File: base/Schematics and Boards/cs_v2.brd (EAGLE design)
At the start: 25.4 x 25.4 mm, 81 parts, among them J101 J-JTAG-CORTEX-NEEDLE6, J301 HIROSE-DF40_44-PIN_CONNECTORS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, J302 HIROSE-DF40_30-PIN_CONNECTORS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, Q201 FK3303010L, Q202 FK3303010L, Q203 FK3303010L, Q204 DMG3415UFY4Q-7, U1 AT25SF641-MHB-T, U101 ATSAMD51, U201 COULOMB-MAX17262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

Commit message: Ready to route
interior planes placed, but not exterior. Layering stackup setup similar to the way JLC recommends (hopefully standard)
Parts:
- moved T_RX 12.8 mm to (17.9, 6.60), flipped to the top
- moved T_TX 7.90 mm to (15.1, 6.58), flipped to the top
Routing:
- removed copper zone on layer 15, net +3V3_STOR
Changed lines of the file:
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@@
 <class number="0" name="default" width="0" drill="0">
 </class>
-<class number="1" name="power_3v3" width="0.3048" drill="0">
+<class number="1" name="power_3v3" width="0.254" drill="0">
 </class>
 <class number="5" name="10_mil" width="0.254" drill="0">
@@
 <autorouter>
 <pass name="Default">
-<param name="RoutingGrid" value="50mil"/>
-<param name="AutoGrid" value="1"/>
-<param name="Efforts" value="0"/>
+<param name="RoutingGrid" value="1mil"/>
+<param name="AutoGrid" value="0"/>
+<param name="Efforts" value="2"/>
 <param name="TopRouterVariant" value="1"/>
 <param name="tpViaShape" value="round"/>
 <param name="PrefDir.1" value="a"/>
 <param name="PrefDir.2" value="0"/>
-<param name="PrefDir.3" value="0"/>
+<param name="PrefDir.3" value="*"/>
 <param name="PrefDir.4" value="0"/>
 <param name="PrefDir.5" value="0"/>
@@
 <param name="PrefDir.12" value="0"/>
 <param name="PrefDir.13" value="0"/>
-<param name="PrefDir.14" value="0"/>
+<param name="PrefDir.14" value="*"/>
 <param name="PrefDir.15" value="0"/>
 <param name="PrefDir.16" value="a"/>
@@
 <attribute name="VALUE" x="1.27" y="20.447" size="0.6096" layer="28" font="vector" ratio="20" rot="MR90" align="top-center"/>
 </element>
-<element name="T_RX" library="TestPoints" package="TP06R" package3d_urn="urn:adsk.eagle:package:27954/1" value="TPTP06R" x="6.35" y="1.0668" smashed="yes" rot="MR0">
-<attribute name="NAME" x="7.4016" y="1.635" size="0.8128" layer="26" rot="MR0"/>
-<attribute name="POPULARITY" value="1" x="-20.32" y="-48.4632" size="1.778" layer="28" rot="MR0" display="off"/>
-<attribute name="TP_SIGNAL_NAME" value="" x="6.35" y="-1.4732" size="1" layer="38" rot="MR0"/>
-</element>
-<element name="T_TX" library="TestPoints" package="TP06R" package3d_urn="urn:adsk.eagle:package:27954/1" value="TPTP06R" x="9.652" y="0.8636" smashed="yes" rot="MR0">
-<attribute name="NAME" x="10.7036" y="1.4572" size="0.8128" layer="26" rot="MR0"/>
-<attribute name="POPULARITY" value="1" x="-22.098" y="-48.6664" size="1.778" layer="28" rot="MR0" display="off"/>
-<attribute name="TP_SIGNAL_NAME" value="" x="9.652" y="-1.6764" size="1" layer="38" rot="MR0"/>
+<element name="T_RX" library="TestPoints" package="TP06R" package3d_urn="urn:adsk.eagle:package:27954/1" value="TPTP06R" x="17.907" y="6.604" smashed="yes">
+<attribute name="NAME" x="16.8046" y="7.1468" size="0.8128" layer="25"/>
+<attribute name="POPULARITY" value="1" x="44.577" y="-42.926" size="1.778" layer="27" display="off"/>
+<attribute name="TP_SIGNAL_NAME" value="" x="17.907" y="4.064" size="1" layer="37"/>
+</element>
+<element name="T_TX" library="TestPoints" package="TP06R" package3d_urn="urn:adsk.eagle:package:27954/1" value="TPTP06R" x="15.113" y="6.5786" smashed="yes">
+<attribute name="NAME" x="13.2232" y="7.0198" size="0.8128" layer="25"/>
+<attribute name="POPULARITY" value="1" x="46.863" y="-42.9514" size="1.778" layer="27" display="off"/>
+<attribute name="TP_SIGNAL_NAME" value="" x="15.113" y="4.0386" size="1" layer="37"/>
 </element>
 <element name="U101" library="Processors" package="TFBGA120" value="ATSAMD51" x="16.3068" y="13.1826" smashed="yes" rot="MR90">
@@
 <contactref element="J301" pad="5"/>
 <polygon width="0.1524" layer="2">
-<vertex x="-49.53" y="31.115"/>
-<vertex x="-49.53" y="-0.635"/>
-<vertex x="-16.383" y="-0.635"/>
-<vertex x="-16.383" y="31.115"/>
+<vertex x="-3.81" y="27.94"/>
+<vertex x="-3.81" y="-3.81"/>
+<vertex x="29.337" y="-3.81"/>
+<vertex x="29.337" y="27.94"/>
 </polygon>
 <contactref element="S101" pad="2_2"/>
@@
 <contactref element="U1" pad="4"/>
 <polygon width="0.1524" layer="16">
-<vertex x="-51.435" y="33.02"/>
-<vertex x="-51.435" y="-2.54"/>
-<vertex x="-14.478" y="-2.54"/>
-<vertex x="-14.478" y="33.02"/>
+<vertex x="-57.15" y="33.655"/>
+<vertex x="-57.15" y="-3.175"/>
+<vertex x="-18.288" y="-3.175"/>
+<vertex x="-18.288" y="33.655"/>
 </polygon>
 <polygon width="0.1524" layer="1">
-<vertex x="-47.625" y="29.21"/>
-<vertex x="-47.625" y="0.635"/>
-<vertex x="-18.288" y="0.635"/>
-<vertex x="-18.288" y="29.21"/>
+<vertex x="-52.705" y="29.845"/>
+<vertex x="-52.705" y="1.27"/>
+<vertex x="-23.368" y="1.27"/>
+<vertex x="-23.368" y="29.845"/>
 </polygon>
 <wire x1="21.9274" y1="21.209" x2="20.371" y2="23.9522" width="0" layer="19" extent="1-16"/>
@@
 <contactref element="J302" pad="14"/>
 <polygon width="0.1524" layer="15">
-<vertex x="54.61" y="31.242"/>
-<vertex x="54.61" y="12.7"/>
-<vertex x="76.2" y="12.7"/>
-<vertex x="76.2" y="31.242"/>
+<vertex x="-5.08" y="29.337"/>
+<vertex x="-5.08" y="-5.08"/>
+<vertex x="31.115" y="-5.08"/>
+<vertex x="31.115" y="29.337"/>
 </polygon>
 <contactref element="T_CPU" pad="TP"/>
@@
 <contactref element="U205" pad="B1"/>
 <contactref element="C208" pad="1"/>
-<polygon width="0.1524" layer="15">
-<vertex x="76.2" y="-6.858"/>
-<vertex x="57.404" y="-6.858"/>
-<vertex x="57.404" y="12.319"/>
-<vertex x="76.2" y="12.319"/>
-</polygon>
 <contactref element="U1" pad="8"/>
 <contactref element="T_STR" pad="TP"/>
@@
 <contactref element="J302" pad="15"/>
 <wire x1="15.80681875" y1="10.182603125" x2="16.637003125" y2="24.273" width="0" layer="19" extent="16-16"/>
-<wire x1="9.652" y1="0.8636" x2="15.80681875" y2="10.182603125" width="0" layer="19" extent="16-16"/>
+<wire x1="15.113" y1="6.5786" x2="15.80681875" y2="10.182603125" width="0" layer="19" extent="16-16"/>
 </signal>
 <signal name="DBG_SERIAL_RX">
@@
 <contactref element="J302" pad="17"/>
 <wire x1="15.306821875" y1="9.68260625" x2="17.037003125" y2="24.273" width="0" layer="19" extent="16-16"/>
-<wire x1="6.35" y1="1.0668" x2="15.306821875" y2="9.68260625" width="0" layer="19" extent="16-16"/>
+<wire x1="17.907" y1="6.604" x2="15.306821875" y2="9.68260625" width="0" layer="19" extent="16-16"/>
 </signal>
 <signal name="JTAG_NRESET">
@@
 <wire x1="4.417" y1="18.197" x2="5.969" y2="18.611" width="0" layer="19" extent="16-16"/>
 </signal>
-<signal name="VREG_LX1" class="1">
+<signal name="VREG_LX1">
 <contactref element="U203" pad="A1"/>
 <contactref element="L201" pad="1"/>
 <wire x1="8.3185" y1="12.2428" x2="8.3502" y2="14.8178" width="0" layer="19" extent="16-16"/>
 </signal>
-<signal name="VREG_LX2" class="1">
+<signal name="VREG_LX2">
 <contactref element="L201" pad="2"/>
 <contactref element="U203" pad="C1"/>
 <wire x1="5.8039" y1="12.2428" x2="7.5502" y2="14.8178" width="0" layer="19" extent="16-16"/>
 </signal>
-<signal name="VREG_BIAS" class="1">
+<signal name="VREG_BIAS">
 <contactref element="C204" pad="1"/>
 <contactref element="U203" pad="A3"/>
@@
 <wire x1="19.304" y1="0.7874" x2="8.030003125" y2="4.715" width="0" layer="19" extent="1-1"/>
 </signal>
-<signal name="VDD_DBG_JMP" class="5">
+<signal name="VDD_DBG_JMP" class="1">
 <contactref element="Q204" pad="1"/>
 <contactref element="R204" pad="2"/>
@@
 <wire x1="8.57" y1="20.209" x2="10.3886" y2="22.225" width="0" layer="19" extent="16-16"/>
 </signal>
-<signal name="VREG_IN" class="5">
+<signal name="VREG_IN" class="1">
 <contactref element="U203" pad="A2"/>
 <contactref element="C202" pad="1"/>
@@
 <wire x1="8.0906" y1="15.113" x2="9.6012" y2="15.0368" width="0" layer="19" extent="1-1"/>
 </signal>
-<signal name="+3V3_TEMP" class="1">
+<signal name="+3V3_TEMP">
 <contactref element="U206" pad="A1"/>
 <contactref element="U206" pad="B1"/>
@@
 <wire x1="21.664" y1="13.8684" x2="23.2664" y2="12.3952" width="0" layer="19" extent="1-16"/>
 </signal>
-<signal name="+3V3_TEMP_SENSE" class="1">
+<signal name="+3V3_TEMP_SENSE">
 <contactref element="U206" pad="A2"/>
 <contactref element="U206" pad="B2"/>
@@
 <wire x1="14.637003125" y1="24.273" x2="14.237003125" y2="24.273" width="0" layer="19" extent="16-16"/>
 </signal>
-<signal name="VDD_SW" class="5">
+<signal name="VDD_SW" class="1">
 <contactref element="Q204" pad="2"/>
 <contactref element="U202" pad="N"/>
@@
 <wire x1="15.80681875" y1="9.68260625" x2="14.681" y2="21.4122" width="0" layer="19" extent="1-16"/>
 </signal>
-<signal name="VDD_SW_IN">
+<signal name="VDD_SW_IN" class="1">
 <contactref element="JP1" pad="2"/>
 <contactref element="S201" pad="2"/>

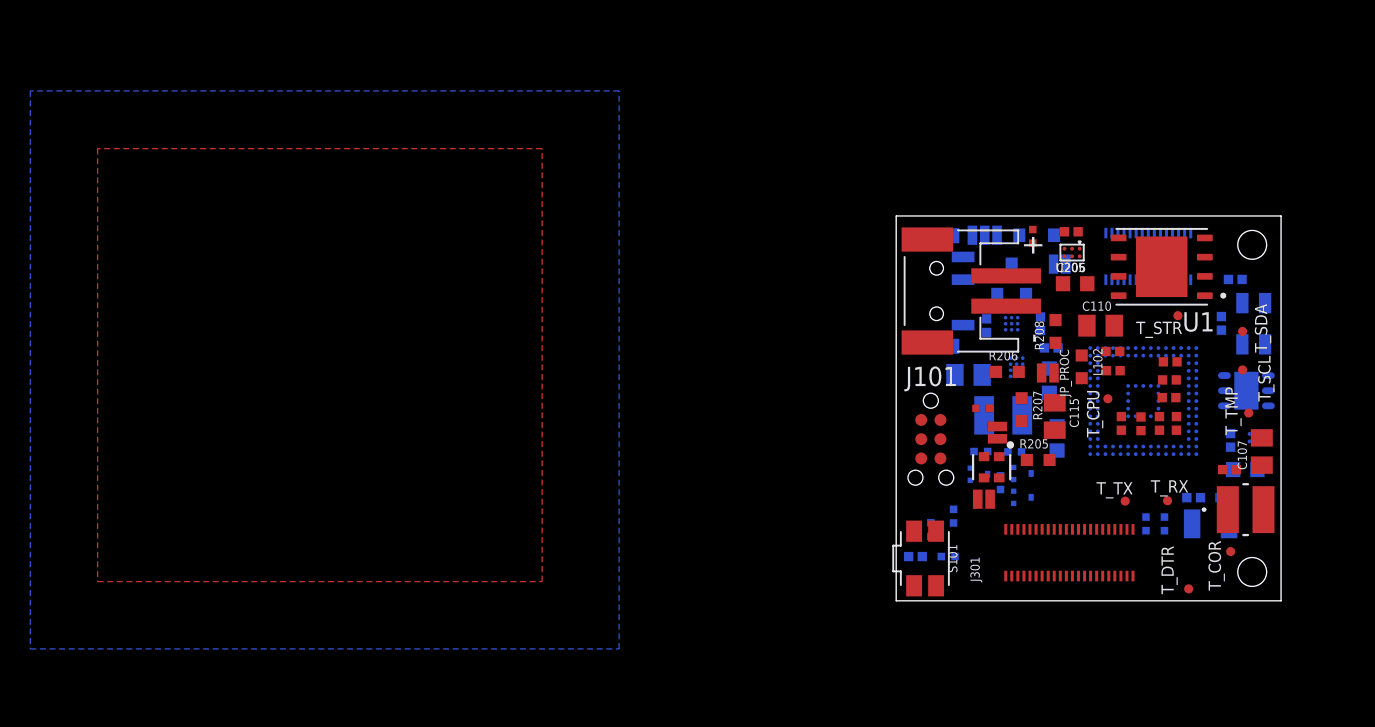
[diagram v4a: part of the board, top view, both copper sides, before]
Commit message: Hand-route power traces and lock signals to prep for autoroute
Moved around some components to give more space for routing from processor to connectors

Hand routed all the power traces with 10mil traces. Should satisfy 6 mil separations, but design will need 5mils to escape all BGA signals. 

Locked traces and vias to prevent ripup from changing them
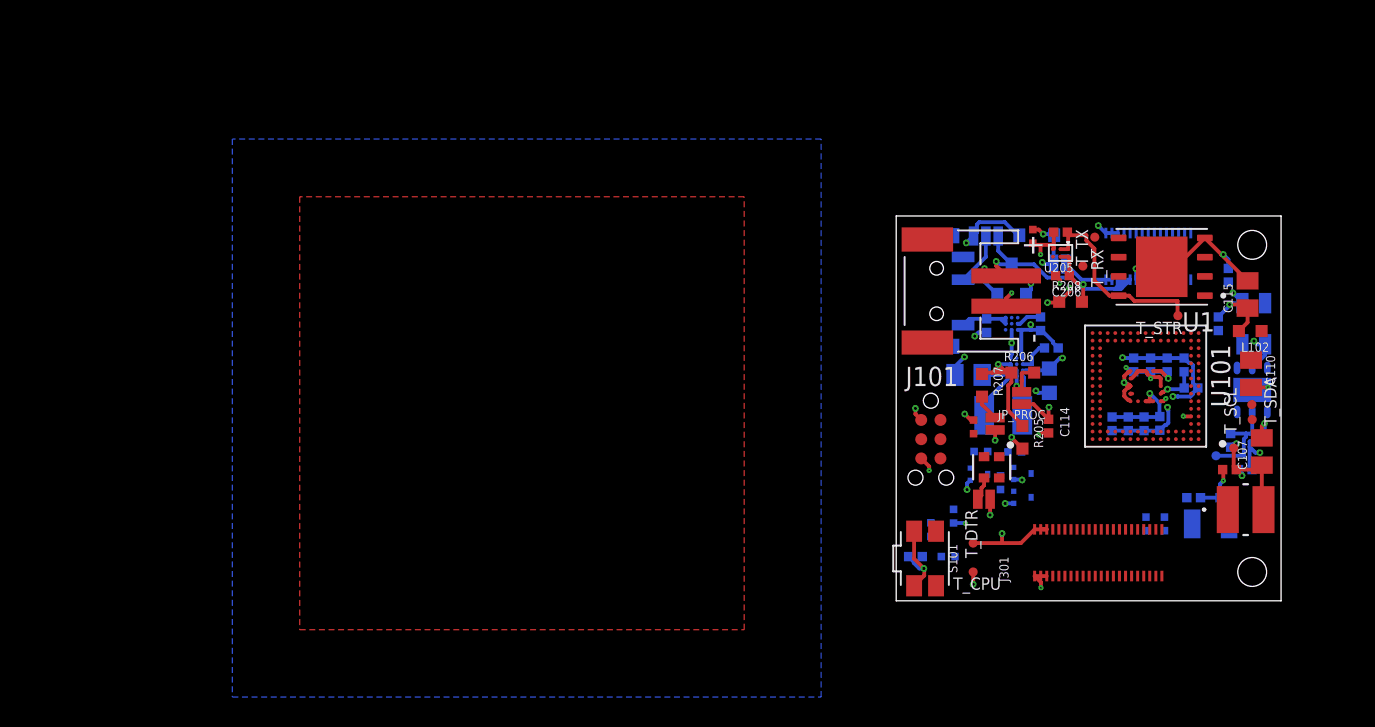
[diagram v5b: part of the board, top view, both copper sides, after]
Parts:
- C114, C206, C207: device Capacitors:C0603 -> Capacitors:C0402
- moved T_TX 17.5 mm to (13.1, 24.0), turned to 90 degrees
- moved T_RX 16.5 mm to (12.3, 22.1), turned to 270 degrees
- moved C115 15.1 mm to (23.2, 20.2), turned to 90 degrees
- moved T_DTR 14.5 mm to (5.08, 3.81)
- moved T_CPU 14.5 mm to (5.08, 1.91), turned to 0 degrees
- moved L102 11.4 mm to (23.4, 17.8), turned to 180 degrees
- moved C110 10.4 mm to (23.4, 15.0), turned to 270 degrees
- moved T_COR 6.84 mm to (22.3, 10.1)
- moved C112 5.61 mm to (14.2, 11.7), flipped to the bottom, turned to 270 degrees
- moved C105 5.26 mm to (19.5, 14.0), flipped to the bottom, turned to 180 degrees
- moved T_SDA 4.86 mm to (23.5, 13.0)
- moved C108 4.78 mm to (19.0, 15.6), flipped to the bottom, turned to 90 degrees
- moved C102 4.32 mm to (16.8, 15.6), flipped to the bottom, turned to 90 degrees
- moved C104 4.25 mm to (17.9, 15.6), flipped to the bottom, turned to 90 degrees
- moved C106 4.22 mm to (15.7, 15.6), flipped to the bottom, turned to 90 degrees
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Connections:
- removed net N$21: J302.1, J302.3, J302.5
- net +3V7_BATT: now also JP1.3; no longer JP1.1
- net GND: now also J302.1, J302.3, J302.5
- net VDD_SW: now also JP1.1; no longer JP1.3
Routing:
- net GND: track 0.00 -> 152.3 mm, vias 0 -> 30
- net +3V3_PROC: track 0.00 -> 67.5 mm, vias 0 -> 12
- net +3V3_TEMP_SENSE: track 0.00 -> 49.3 mm, vias 0 -> 3
- net +3V3_DTR: track 0.00 -> 42.6 mm, vias 0 -> 3
- net +3V3: track 0.00 -> 28.2 mm, vias 0 -> 4
- net +3V7_BATT: track 0.00 -> 17.2 mm, vias 0 -> 1
- net +3V3_STOR: track 0.00 -> 13.2 mm
- net +3V3_STOR_SENSE: track 0.00 -> 10.4 mm, vias 0 -> 2
- net VDD_SW: track 0.00 -> 9.00 mm, vias 0 -> 2
- net VREG_IN: track 0.00 -> 8.45 mm, vias 0 -> 2
- net VDD_DBG_JMP: track 0.00 -> 6.87 mm, vias 0 -> 3
- net +3V3_TEMP: track 0.00 -> 6.55 mm
- net VDDCORE: track 0.00 -> 6.28 mm
- net CC_IN: track 0.00 -> 3.83 mm
- net VDD_SW_IN: track 0.00 -> 3.50 mm
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
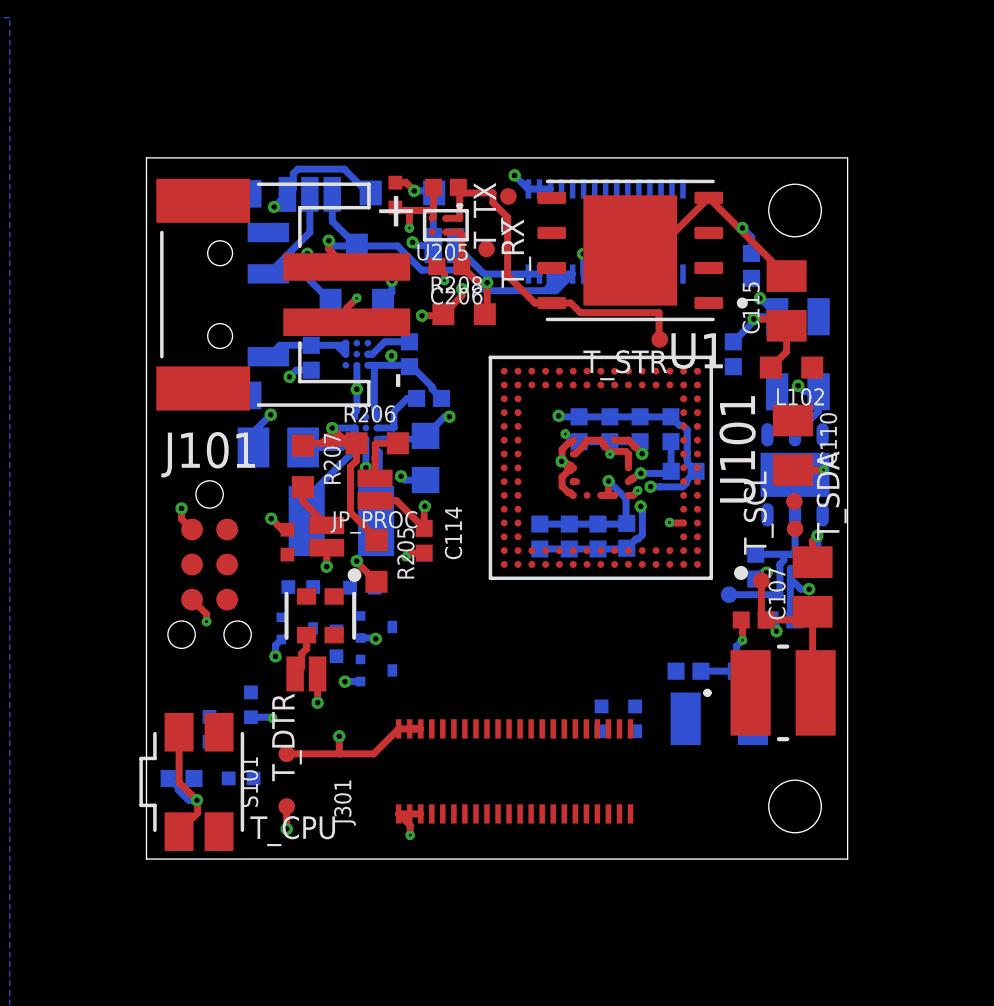
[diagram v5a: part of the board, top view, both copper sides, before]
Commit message: Updated stackup for 8-layer. Added feasible via pairs
My understanding of viable via pairs is still a bit shaky (or at least what proto express can do). I have designed to have a few pairs of micro vias, and through hole plating for each core-to-core layer, which should be doable for 3-step lamination process
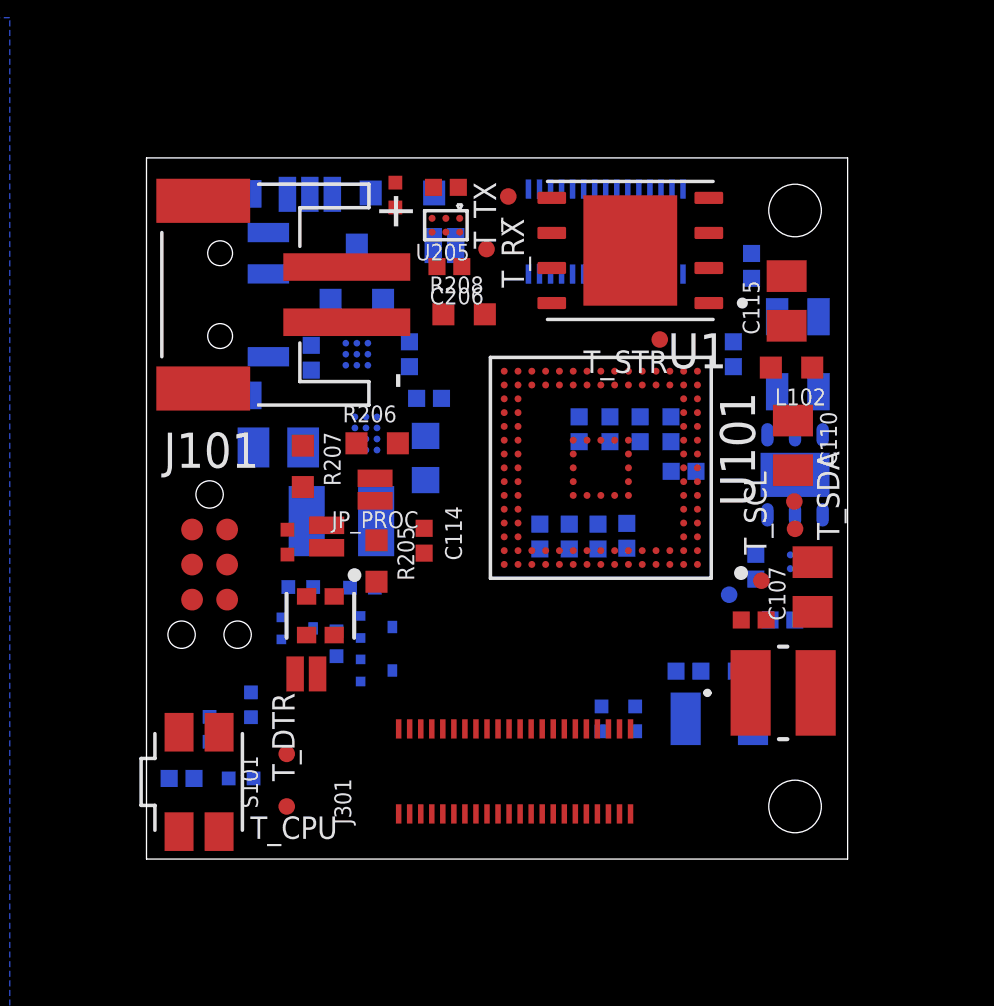
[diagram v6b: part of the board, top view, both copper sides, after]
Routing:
- net GND: track 152.3 -> 0.00 mm, vias 30 -> 0
- net +3V3_PROC: track 67.5 -> 0.00 mm, vias 12 -> 0
- net +3V3_TEMP_SENSE: track 49.3 -> 0.00 mm, vias 3 -> 0
- net +3V3_DTR: track 42.6 -> 0.00 mm, vias 3 -> 0
- net +3V3: track 28.2 -> 0.00 mm, vias 4 -> 0
- net +3V7_BATT: track 17.2 -> 0.00 mm, vias 1 -> 0
- net +3V3_STOR: track 13.2 -> 0.00 mm
- net +3V3_STOR_SENSE: track 10.4 -> 0.00 mm, vias 2 -> 0
- net VDD_SW: track 9.00 -> 0.00 mm, vias 2 -> 0
- net VREG_IN: track 8.45 -> 0.00 mm, vias 2 -> 0
- net VDD_DBG_JMP: track 6.87 -> 0.00 mm, vias 3 -> 0
- net +3V3_TEMP: track 6.55 -> 0.00 mm
- net VDDCORE: track 6.28 -> 0.00 mm
- net CC_IN: track 3.83 -> 0.00 mm
- net VDD_SW_IN: track 3.50 -> 0.00 mm
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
